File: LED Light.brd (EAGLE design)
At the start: 78.7 x 78.7 mm, 9 parts, among them J1 AVR_SPI_PRG_6NS, U1 Tiny85-20-SMT

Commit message: Night-light lamp, including PNGs for milling and PDFs for laser-cutting.
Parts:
- added LED1: ML-EFAB, LED Light:ML-E-FAB
- added R4: (no value), rcl:R1206
- added R6: 49.9K, rcl:R1206
- added U$1: PHOTOTRANSISTOR-NPN-OP580AD, LED Light:OP580DA
- moved R1 31.8 mm to (44.5, 19.7)
- moved U1 31.8 mm to (44.5, 15.2)
- moved C1 31.8 mm to (43.2, 11.4)
- moved R3 31.3 mm to (36.2, 12.7), turned to 270 degrees
- moved JP1 30.5 mm to (50.8, 4.45)
- moved J1 30.5 mm to (59.7, 15.2)
- moved LED2 26.9 mm to (30.5, 20.3), turned to 180 degrees
- moved T1 22.1 mm to (34.3, 8.26), turned to 180 degrees
- moved R2 16.9 mm to (29.2, 9.53), turned to 0 degrees
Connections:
- new net N$5: LED1.A@1, R4.1
- new net N$7: R6.1, U$1.COLLECTOR, U1.2
- net GND: now also LED1.C@1, U$1.EMITTER
- net N$1: now also R4.2
- net VCC: now also R6.2
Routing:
- net N$5: track 0.00 -> 109.9 mm
- net N$3: track 76.9 -> 18.9 mm
- net N$7: track 0.00 -> 49.7 mm
- net GND: track 127.3 -> 172.6 mm
- net N$2: track 38.9 -> 2.88 mm
- net VCC: track 48.8 -> 55.7 mm
- net N$1: track 2.69 -> 5.42 mm
- net SCK: track 31.6 -> 29.0 mm
- net MISO: track 22.7 -> 20.1 mm
- net RESET: track 51.7 -> 50.4 mm
- net MOSI: track 13.8 -> 12.5 mm
- net N$4: track 4.24 -> 4.98 mm
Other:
- board size 78.7 x 78.7 mm -> 101.6 x 55.9 mm

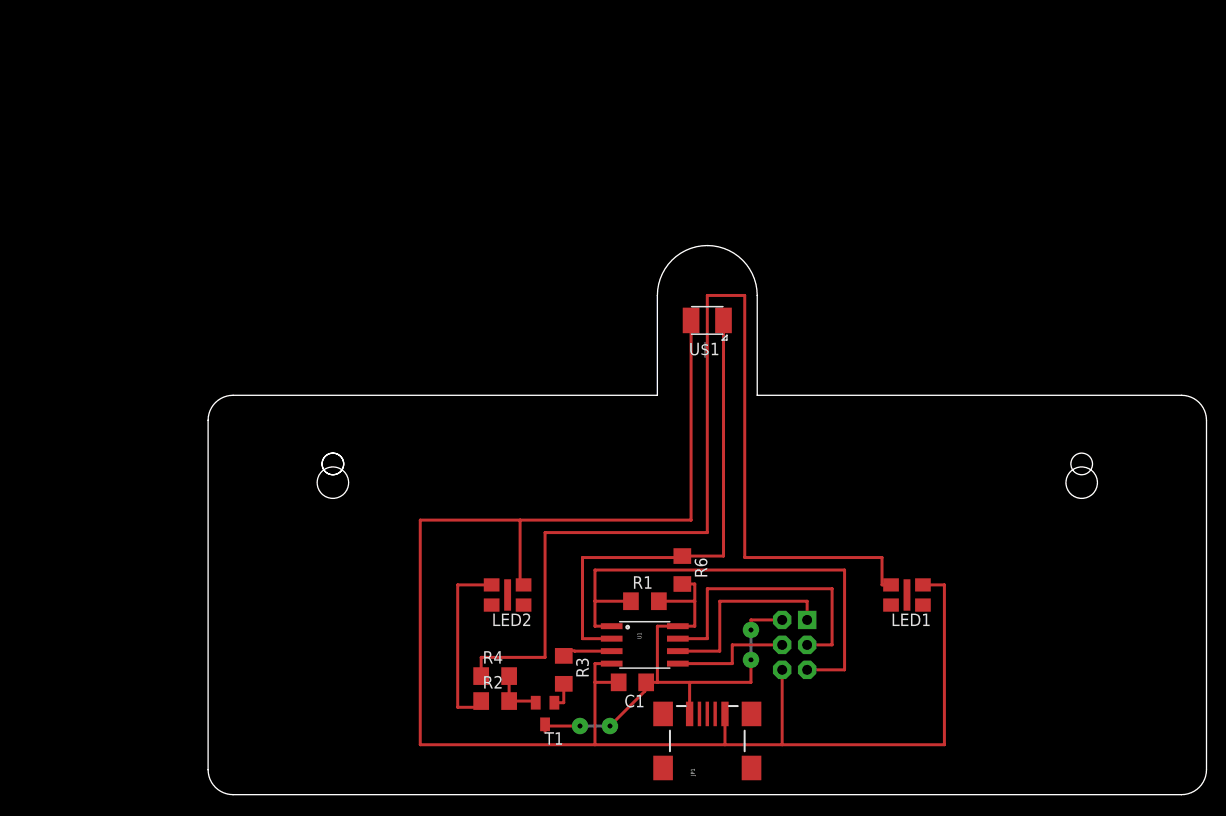
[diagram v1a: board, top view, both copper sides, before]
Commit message: Replace Mini-B USB connector w/ male A. Switch LEDs to PB1 (MISO). Layout.
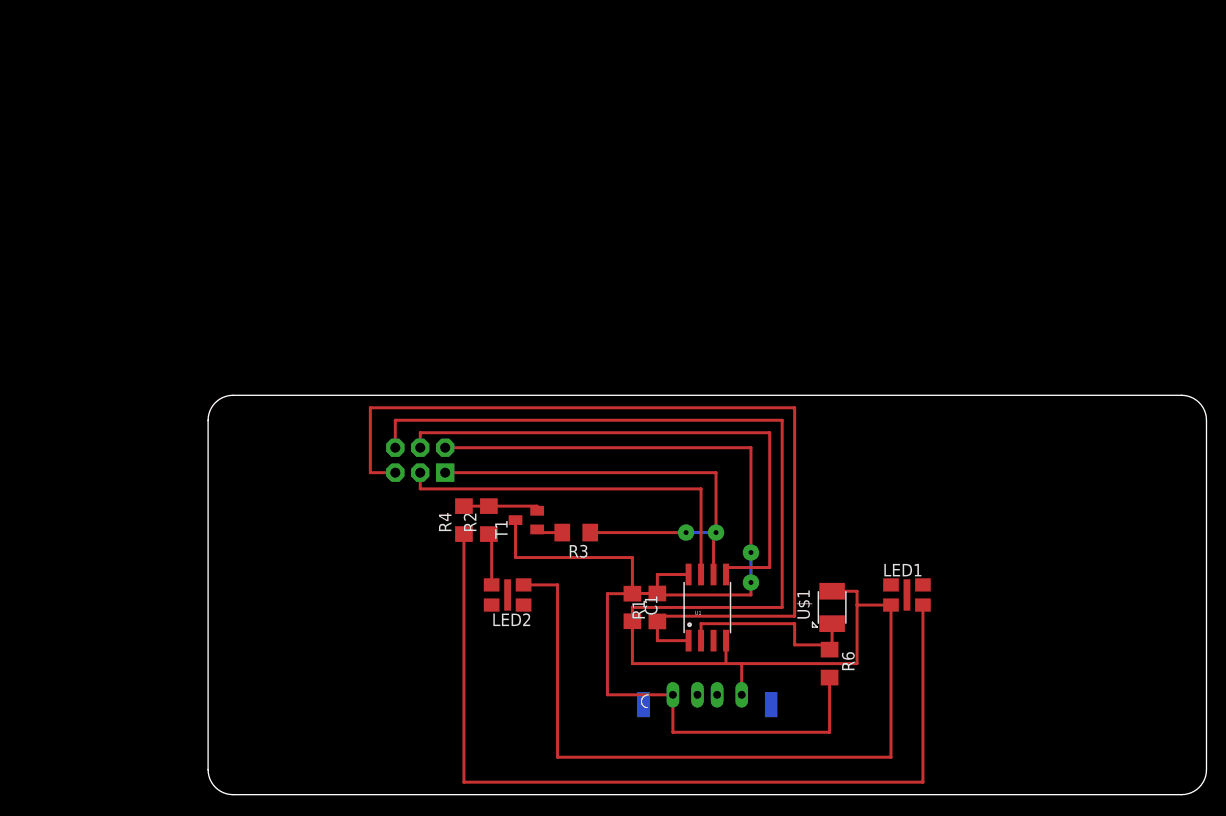
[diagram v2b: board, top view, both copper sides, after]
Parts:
- JP1: value USB_MINIB-POWER -> USB_A_VERTICAL; device LED Light:USB_MINIB_POWER -> LED Light:USB_A_VERTICAL
- moved J1 42.5 mm to (21.6, 34.0), turned to 0 degrees
- moved U$1 31.9 mm to (63.5, 19.1), turned to 90 degrees
- moved T1 19.8 mm to (32.4, 27.9), turned to 90 degrees
- moved R2 18.4 mm to (28.6, 27.9), turned to 90 degrees
- moved R6 17.8 mm to (63.2, 13.3)
- moved R4 16.2 mm to (26.0, 27.9), turned to 90 degrees
- moved R3 14.0 mm to (37.5, 26.7), turned to 180 degrees
- moved C1 7.62 mm to (43.2, 19.1), turned to 270 degrees
- moved U1 7.41 mm to (50.8, 19.1), turned to 0 degrees
- moved JP1 5.71 mm to (50.8, 10.2), flipped to the bottom, turned to 0 degrees
- moved R1 1.42 mm to (45.7, 19.1), turned to 90 degrees
- turned LED1 to 0 degrees
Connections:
- removed net N$4: R3.1, U1.3
- net MISO: now also R3.1
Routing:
- net VCC: track 55.7 -> 127.6 mm, vias 4 -> 2
- net MOSI: track 12.5 -> 56.0 mm
- net RESET: track 50.4 -> 93.2 mm
- net MISO: track 20.1 -> 51.0 mm, vias 0 -> 2
- net N$7: track 49.7 -> 20.3 mm
- net GND: track 172.6 -> 194.3 mm
- net N$5: track 109.9 -> 90.0 mm
- net N$3: track 18.9 -> 5.45 mm
- net SCK: track 29.0 -> 38.9 mm
- net N$4: track 4.98 -> 0.00 mm
- net N$1: track 5.42 -> 7.92 mm
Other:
- board size 101.6 x 55.9 mm -> 101.6 x 40.6 mm

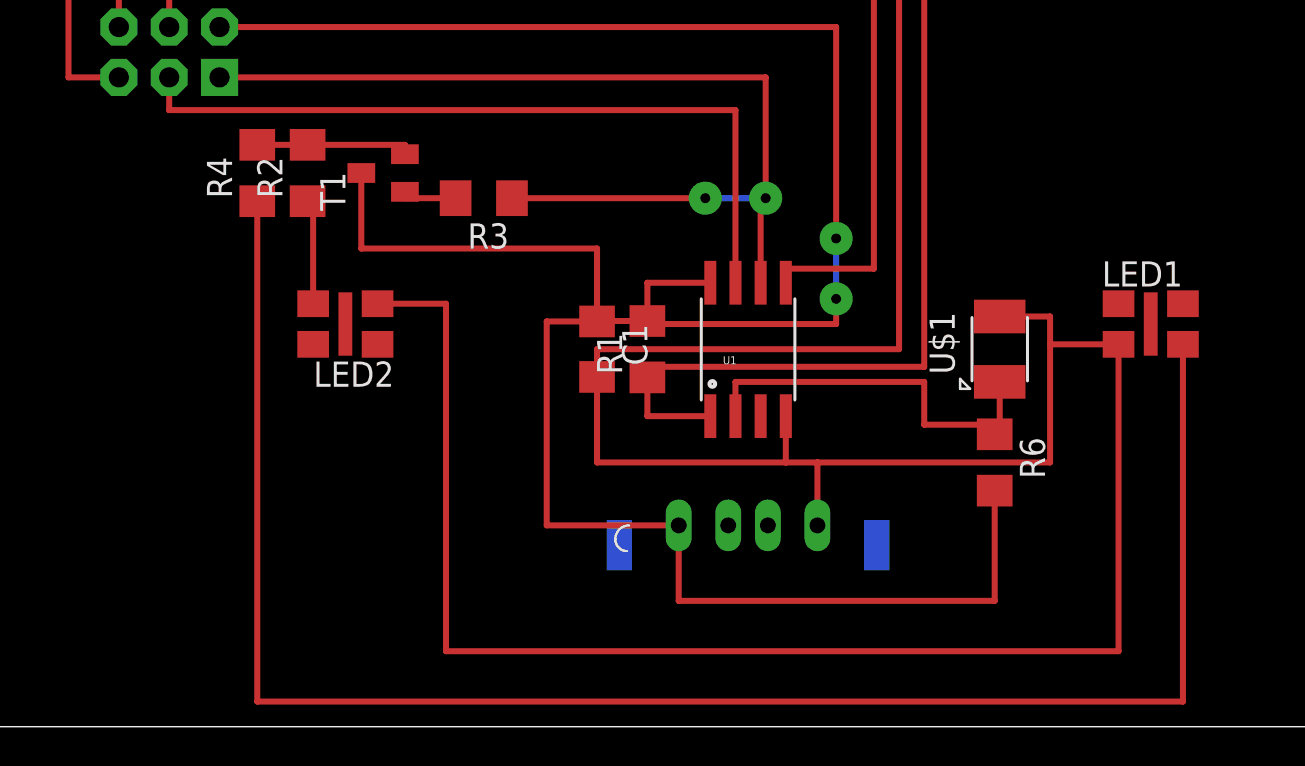
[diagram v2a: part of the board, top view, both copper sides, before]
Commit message: Tweak board layout, generate PNGs for milling.
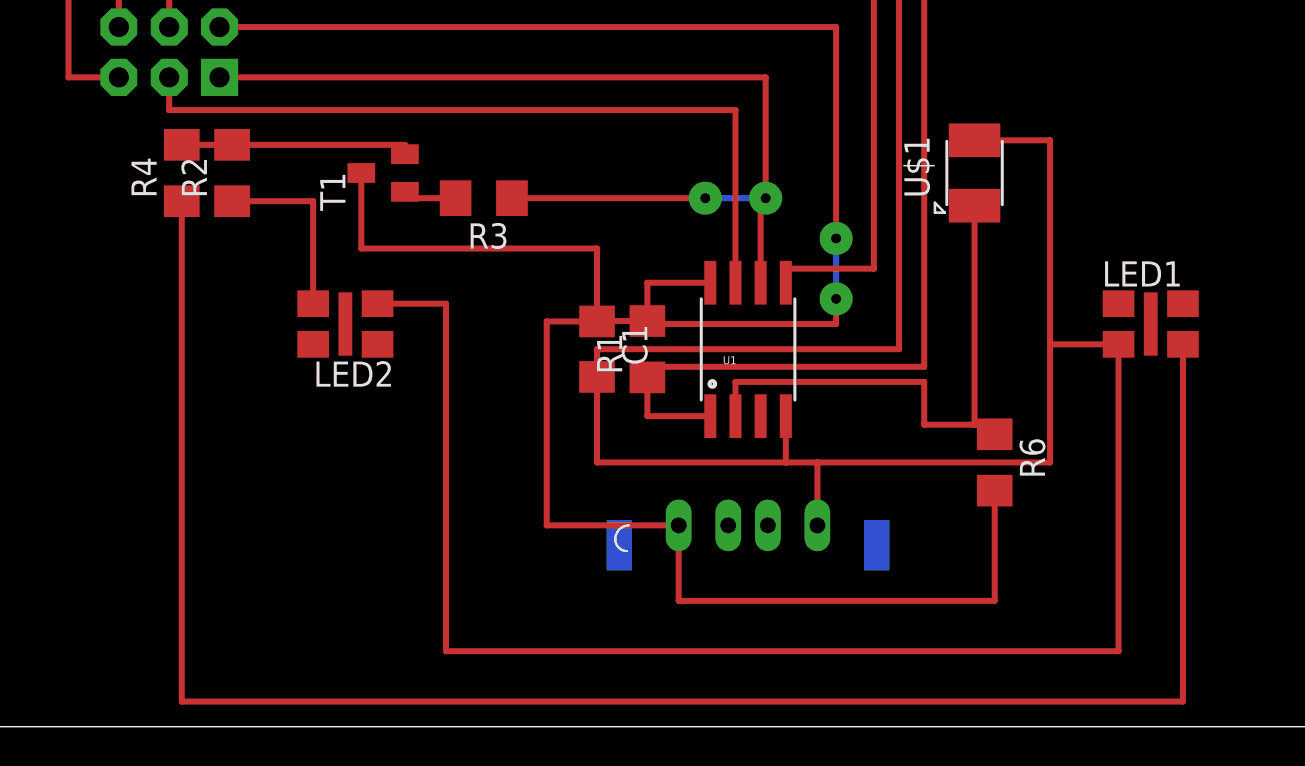
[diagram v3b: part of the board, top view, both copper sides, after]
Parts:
- moved U$1 8.98 mm to (62.2, 27.9)
- moved R2 3.81 mm to (24.8, 27.9)
- moved R4 3.81 mm to (22.2, 27.9)
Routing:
- net GND: track 194.3 -> 204.5 mm
- net N$7: track 20.3 -> 28.5 mm
- net N$5: track 90.0 -> 93.8 mm
- net N$3: track 5.45 -> 9.26 mm
- net N$1: track 7.92 -> 11.7 mm
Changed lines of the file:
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@@
 <layer number="14" name="Route14" color="1" fill="6" visible="no" active="no"/>
 <layer number="15" name="Route15" color="4" fill="6" visible="no" active="no"/>
-<layer number="16" name="Bottom" color="1" fill="1" visible="yes" active="yes"/>
+<layer number="16" name="Bottom" color="1" fill="1" visible="no" active="yes"/>
 <layer number="17" name="Pads" color="2" fill="1" visible="yes" active="yes"/>
 <layer number="18" name="Vias" color="2" fill="1" visible="yes" active="yes"/>
-<layer number="19" name="Unrouted" color="6" fill="1" visible="yes" active="yes"/>
-<layer number="20" name="Dimension" color="15" fill="1" visible="yes" active="yes"/>
-<layer number="21" name="tPlace" color="7" fill="1" visible="yes" active="yes"/>
-<layer number="22" name="bPlace" color="7" fill="1" visible="yes" active="yes"/>
-<layer number="23" name="tOrigins" color="15" fill="1" visible="yes" active="yes"/>
-<layer number="24" name="bOrigins" color="15" fill="1" visible="yes" active="yes"/>
-<layer number="25" name="tNames" color="7" fill="1" visible="yes" active="yes"/>
-<layer number="26" name="bNames" color="7" fill="1" visible="yes" active="yes"/>
-<layer number="27" name="tValues" color="7" fill="1" visible="yes" active="yes"/>
-<layer number="28" name="bValues" color="7" fill="1" visible="yes" active="yes"/>
+<layer number="19" name="Unrouted" color="6" fill="1" visible="no" active="yes"/>
+<layer number="20" name="Dimension" color="15" fill="1" visible="no" active="yes"/>
+<layer number="21" name="tPlace" color="7" fill="1" visible="no" active="yes"/>
+<layer number="22" name="bPlace" color="7" fill="1" visible="no" active="yes"/>
+<layer number="23" name="tOrigins" color="15" fill="1" visible="no" active="yes"/>
+<layer number="24" name="bOrigins" color="15" fill="1" visible="no" active="yes"/>
+<layer number="25" name="tNames" color="7" fill="1" visible="no" active="yes"/>
+<layer number="26" name="bNames" color="7" fill="1" visible="no" active="yes"/>
+<layer number="27" name="tValues" color="7" fill="1" visible="no" active="yes"/>
+<layer number="28" name="bValues" color="7" fill="1" visible="no" active="yes"/>
 <layer number="29" name="tStop" color="7" fill="3" visible="no" active="yes"/>
 <layer number="30" name="bStop" color="7" fill="6" visible="no" active="yes"/>
@@
 <layer number="42" name="bRestrict" color="1" fill="10" visible="no" active="yes"/>
 <layer number="43" name="vRestrict" color="2" fill="10" visible="no" active="yes"/>
-<layer number="44" name="Drills" color="7" fill="1" visible="yes" active="yes"/>
-<layer number="45" name="Holes" color="7" fill="1" visible="yes" active="yes"/>
+<layer number="44" name="Drills" color="7" fill="1" visible="no" active="yes"/>
+<layer number="45" name="Holes" color="7" fill="1" visible="no" active="yes"/>
 <layer number="46" name="Milling" color="3" fill="1" visible="no" active="yes"/>
 <layer number="47" name="Measures" color="7" fill="1" visible="no" active="yes"/>
@@
 <layer number="112" name="tSilk" color="7" fill="1" visible="no" active="yes"/>
 <layer number="113" name="IDFDebug" color="7" fill="1" visible="no" active="yes"/>
-<layer number="114" name="AcrylicBase" color="11" fill="1" visible="yes" active="yes"/>
+<layer number="114" name="AcrylicBase" color="11" fill="1" visible="no" active="yes"/>
 <layer number="115" name="AcrylicCover" color="14" fill="1" visible="no" active="yes"/>
 <layer number="116" name="Patch_BOT" color="9" fill="4" visible="no" active="yes"/>
@@
 <wire x1="101.6" y1="38.1" x2="99.06" y2="40.64" width="0" layer="115" curve="90"/>
 <rectangle x1="-2.54" y1="-2.54" x2="104.14" y2="43.18" layer="48"/>
+<wire x1="11.43" y1="36.83" x2="83.82" y2="36.83" width="0" layer="114"/>
+<wire x1="83.82" y1="36.83" x2="83.82" y2="3.81" width="0" layer="114"/>
+<wire x1="83.82" y1="3.81" x2="11.43" y2="3.81" width="0" layer="114"/>
+<wire x1="11.43" y1="3.81" x2="11.43" y2="36.83" width="0" layer="114"/>
 </plain>
 <attributes>
@@
 <element name="J1" library="SparkFun-Connectors" package="2X3-NS" value="AVR_SPI_PRG_6NS" x="21.59" y="34.036" rot="MR0"/>
 <element name="R1" library="rcl" package="R1206" value="10K" x="45.72" y="19.05" rot="R90"/>
-<element name="R2" library="rcl" package="R1206" value="" x="28.575" y="27.94" rot="R90"/>
+<element name="R2" library="rcl" package="R1206" value="" x="24.765" y="27.94" rot="R90"/>
 <element name="JP1" library="LED Light" package="USB_A_VERTICAL" value="USB_A_VERTICAL" x="50.8" y="10.16" rot="MR0"/>
 <element name="C1" library="rcl" package="C1206" value="1.0uF" x="43.18" y="19.05" rot="R270"/>
@@
 <element name="T1" library="transistor" package="SOT23-BEC" value="" x="32.385" y="27.94" rot="R90"/>
 <element name="R3" library="rcl" package="R1206" value="1K" x="37.465" y="26.67" rot="R180"/>
-<element name="R4" library="rcl" package="R1206" value="" x="26.035" y="27.94" rot="R90"/>
+<element name="R4" library="rcl" package="R1206" value="" x="22.225" y="27.94" rot="R90"/>
 <element name="LED1" library="LED Light" package="ML-E-FAB" value="ML-EFAB" x="71.12" y="20.32"/>
-<element name="U$1" library="LED Light" package="OP580DA" value="PHOTOTRANSISTOR-NPN-OP580AD" x="63.5" y="19.05" rot="R90"/>
+<element name="U$1" library="LED Light" package="OP580DA" value="PHOTOTRANSISTOR-NPN-OP580AD" x="62.23" y="27.94" rot="R90"/>
 <element name="R6" library="rcl" package="R1206" value="49.9K" x="63.246" y="13.335" rot="R270"/>
 </elements>
@@
 <wire x1="43.18" y1="19.05" x2="58.42" y2="19.05" width="0.3048" layer="1"/>
 <wire x1="58.42" y1="38.1" x2="58.42" y2="19.05" width="0.3048" layer="1"/>
-<wire x1="63.5" y1="20.7" x2="66.04" y2="20.7" width="0.3048" layer="1"/>
-<wire x1="66.04" y1="20.7" x2="66.04" y2="19.295" width="0.3048" layer="1"/>
+<wire x1="62.23" y1="29.59" x2="66.04" y2="29.59" width="0.3048" layer="1"/>
+<wire x1="66.04" y1="29.59" x2="66.04" y2="19.295" width="0.3048" layer="1"/>
 <wire x1="66.04" y1="19.295" x2="66.04" y2="13.335" width="0.3048" layer="1"/>
 <wire x1="66.04" y1="13.335" x2="54.3" y2="13.335" width="0.3048" layer="1"/>
@@
 <contactref element="LED2" pad="A@1"/>
 <wire x1="28.855" y1="21.345" x2="28.855" y2="26.518" width="0.3048" layer="1"/>
-<wire x1="28.855" y1="26.518" x2="28.575" y2="26.518" width="0.3048" layer="1"/>
+<wire x1="28.855" y1="26.518" x2="24.765" y2="26.518" width="0.3048" layer="1"/>
 </signal>
 <signal name="N$1">
@@
 <contactref element="T1" pad="E"/>
 <contactref element="R4" pad="2"/>
-<wire x1="28.575" y1="29.362" x2="26.035" y2="29.362" width="0.3048" layer="1"/>
+<wire x1="24.765" y1="29.362" x2="22.225" y2="29.362" width="0.3048" layer="1"/>
 <wire x1="33.485" y1="28.89" x2="33.485" y2="29.362" width="0.3048" layer="1"/>
-<wire x1="33.485" y1="29.362" x2="28.575" y2="29.362" width="0.3048" layer="1"/>
+<wire x1="33.485" y1="29.362" x2="24.765" y2="29.362" width="0.3048" layer="1"/>
 </signal>
 <signal name="N$2">
@@
 <contactref element="LED1" pad="A@1"/>
 <wire x1="72.745" y1="1.27" x2="72.745" y2="19.295" width="0.3048" layer="1"/>
-<wire x1="26.035" y1="26.518" x2="26.035" y2="1.27" width="0.3048" layer="1"/>
-<wire x1="26.035" y1="1.27" x2="72.745" y2="1.27" width="0.3048" layer="1"/>
+<wire x1="22.225" y1="26.518" x2="22.225" y2="1.27" width="0.3048" layer="1"/>
+<wire x1="22.225" y1="1.27" x2="72.745" y2="1.27" width="0.3048" layer="1"/>
 </signal>
 <signal name="N$7">
@@
 <wire x1="50.165" y1="15.6718" x2="50.165" y2="17.399" width="0.3048" layer="1"/>
 <wire x1="50.165" y1="17.399" x2="59.69" y2="17.399" width="0.3048" layer="1"/>
-<wire x1="63.246" y1="14.757" x2="63.5" y2="14.757" width="0.3048" layer="1"/>
-<wire x1="63.5" y1="14.757" x2="63.5" y2="17.4" width="0.3048" layer="1"/>
 <wire x1="59.69" y1="17.399" x2="59.69" y2="15.24" width="0.3048" layer="1"/>
-<wire x1="59.69" y1="15.24" x2="63.246" y2="15.24" width="0.3048" layer="1"/>
+<wire x1="59.69" y1="15.24" x2="62.23" y2="15.24" width="0.3048" layer="1"/>
 <wire x1="63.246" y1="15.24" x2="63.246" y2="14.757" width="0.3048" layer="1"/>
+<wire x1="63.246" y1="15.24" x2="62.23" y2="15.24" width="0.3048" layer="1"/>
+<wire x1="62.23" y1="15.24" x2="62.23" y2="26.29" width="0.3048" layer="1"/>
 </signal>
 </signals>
